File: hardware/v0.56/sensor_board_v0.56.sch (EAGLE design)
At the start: 67 parts, among them J3 USB-MICROB, U1 NEOPIXEL_NANO_2427, U10 TSL2591, U11 915MHz, U12 MH-Z19, U13 CCS811-I2C, U14 IAQ-CORE-C, U15 VLP-450-F, U16 VLP-450-F, U2 FT231XQ-R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

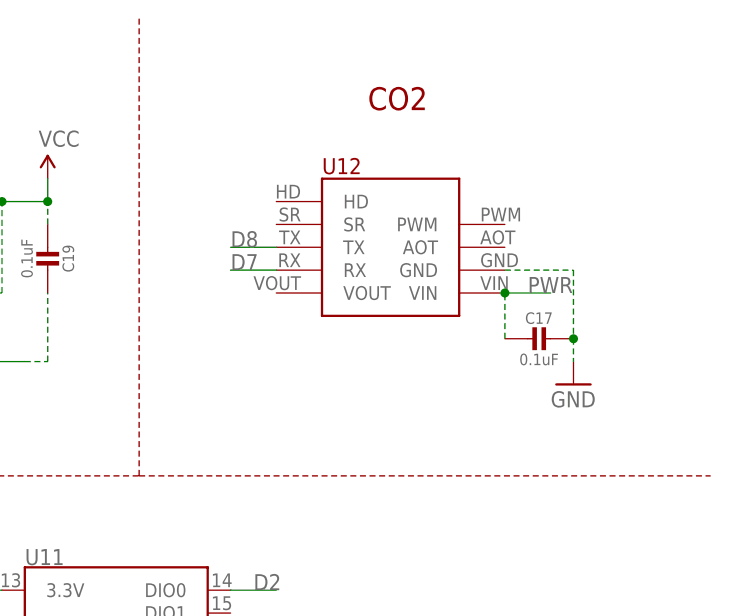
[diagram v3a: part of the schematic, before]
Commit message: Updated v0.56b with SMD pads for MH-z19 sensor
- other minor trace, parts and silkscreen adjustments
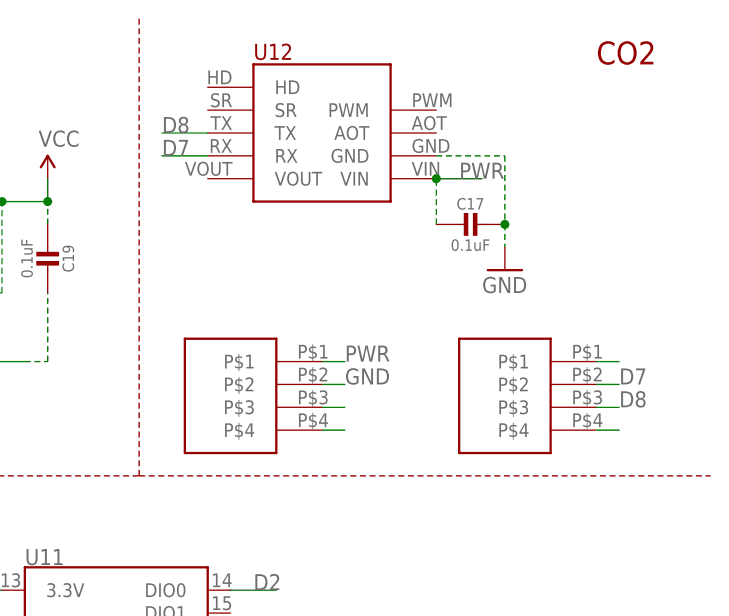
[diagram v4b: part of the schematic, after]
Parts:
- added U$4, U$5: 0878980426, 0878980426:0878980426
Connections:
- new net N$12: U$4.P$4
- new net N$14: U$5.P$1
- new net N$19: U$5.P$4
- new net N$8: U$4.P$3
- net D7: now also U$5.P$2
- net D8: now also U$5.P$3
- net GND: now also U$4.P$2
- net PWR: now also U$4.P$1
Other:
- moved on the sheet: C17, U12
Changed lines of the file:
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@@
 <part name="R10" library="Adafruit Feather 32u4 Bluefruit LE" deviceset="MICROBUILDER_RESISTOR" device="_0402MP" value="10K"/>
 <part name="SUPPLY18" library="SparkFun-Aesthetics" deviceset="VCC" device=""/>
+<part name="U$4" library="0878980426" deviceset="0878980426" device=""/>
+<part name="U$5" library="0878980426" deviceset="0878980426" device=""/>
 </parts>
 <sheets>
@@
 <wire x1="218.44" y1="-66.04" x2="218.44" y2="-12.7" width="0.1524" layer="94" style="longdash"/>
 <wire x1="251.46" y1="88.9" x2="251.46" y2="139.7" width="0.1524" layer="94" style="longdash"/>
-<text x="276.86" y="129.54" size="2.54" layer="94" font="vector">CO2</text>
+<text x="302.26" y="134.62" size="2.54" layer="94" font="vector">CO2</text>
 <wire x1="218.44" y1="-66.04" x2="312.42" y2="-66.04" width="0.1524" layer="94" style="longdash"/>
 <wire x1="53.34" y1="-12.7" x2="53.34" y2="43.18" width="0.1524" layer="94" style="longdash"/>
@@
 <instance part="R20" gate="G$1" x="172.72" y="-55.88" rot="R180"/>
 <instance part="J2" gate="G$1" x="157.48" y="-5.08"/>
-<instance part="U12" gate="G$1" x="279.4" y="114.3">
-<attribute name="MPN" x="279.4" y="114.3" size="1.778" layer="96" display="off"/>
+<instance part="U12" gate="G$1" x="271.78" y="127">
+<attribute name="MPN" x="271.78" y="127" size="1.778" layer="96" display="off"/>
 </instance>
 <instance part="U5" gate="G$1" x="-7.62" y="-71.12"/>
@@
 <instance part="C16" gate="G$1" x="10.16" y="111.76" rot="R180"/>
 <instance part="U13" gate="G$1" x="71.12" y="0"/>
-<instance part="GND14" gate="1" x="299.72" y="99.06"/>
-<instance part="C17" gate="G$1" x="294.64" y="104.14" rot="R270"/>
+<instance part="GND14" gate="1" x="292.1" y="111.76"/>
+<instance part="C17" gate="G$1" x="287.02" y="116.84" rot="R270"/>
 <instance part="JP1" gate="G$1" x="269.24" y="66.04" rot="R90"/>
 <instance part="U1" gate="G$1" x="147.32" y="63.5"/>
@@
 <instance part="R10" gate="G$1" x="101.6" y="99.06" rot="R90"/>
 <instance part="SUPPLY18" gate="G$1" x="111.76" y="96.52"/>
+<instance part="U$4" gate="G$1" x="259.08" y="101.6"/>
+<instance part="U$5" gate="G$1" x="289.56" y="101.6"/>
 </instances>
 <busses>
@@
 <pinref part="U12" gate="G$1" pin="GND"/>
 <pinref part="GND14" gate="1" pin="GND"/>
-<wire x1="292.1" y1="111.76" x2="299.72" y2="111.76" width="0.1524" layer="91" style="longdash"/>
-<wire x1="299.72" y1="111.76" x2="299.72" y2="104.14" width="0.1524" layer="91" style="longdash"/>
+<wire x1="284.48" y1="124.46" x2="292.1" y2="124.46" width="0.1524" layer="91" style="longdash"/>
+<wire x1="292.1" y1="124.46" x2="292.1" y2="116.84" width="0.1524" layer="91" style="longdash"/>
 <pinref part="C17" gate="G$1" pin="1"/>
-<wire x1="299.72" y1="104.14" x2="299.72" y2="101.6" width="0.1524" layer="91" style="longdash"/>
-<junction x="299.72" y="104.14"/>
+<wire x1="292.1" y1="116.84" x2="292.1" y2="114.3" width="0.1524" layer="91" style="longdash"/>
+<junction x="292.1" y="116.84"/>
 </segment>
 <segment>
@@
 <pinref part="C5" gate="G$1" pin="1"/>
 <wire x1="38.1" y1="-78.74" x2="38.1" y2="-76.2" width="0.1524" layer="91"/>
+</segment>
+<segment>
+<pinref part="U$4" gate="G$1" pin="P$2"/>
+<wire x1="271.78" y1="99.06" x2="274.32" y2="99.06" width="0.1524" layer="91"/>
+<label x="274.32" y="99.06" size="1.778" layer="95"/>
 </segment>
 </net>
@@
 <segment>
 <pinref part="U12" gate="G$1" pin="VIN"/>
-<label x="294.64" y="109.22" size="1.778" layer="95"/>
-<wire x1="292.1" y1="109.22" x2="297.18" y2="109.22" width="0.1524" layer="91"/>
+<label x="287.02" y="121.92" size="1.778" layer="95"/>
+<wire x1="284.48" y1="121.92" x2="289.56" y2="121.92" width="0.1524" layer="91"/>
 <pinref part="C17" gate="G$1" pin="2"/>
-<wire x1="292.1" y1="104.14" x2="292.1" y2="109.22" width="0.1524" layer="91" style="longdash"/>
-<junction x="292.1" y="109.22"/>
+<wire x1="284.48" y1="116.84" x2="284.48" y2="121.92" width="0.1524" layer="91" style="longdash"/>
+<junction x="284.48" y="121.92"/>
+</segment>
+<segment>
+<pinref part="U$4" gate="G$1" pin="P$1"/>
+<wire x1="271.78" y1="101.6" x2="274.32" y2="101.6" width="0.1524" layer="91"/>
+<label x="274.32" y="101.6" size="1.778" layer="95"/>
 </segment>
 </net>
@@
 <segment>
 <pinref part="U12" gate="G$1" pin="RX"/>
-<wire x1="266.7" y1="111.76" x2="261.62" y2="111.76" width="0.1524" layer="91"/>
-<label x="261.62" y="111.76" size="1.778" layer="95"/>
+<wire x1="259.08" y1="124.46" x2="254" y2="124.46" width="0.1524" layer="91"/>
+<label x="254" y="124.46" size="1.778" layer="95"/>
+</segment>
+<segment>
+<pinref part="U$5" gate="G$1" pin="P$2"/>
+<wire x1="302.26" y1="99.06" x2="304.8" y2="99.06" width="0.1524" layer="91"/>
+<label x="304.8" y="99.06" size="1.778" layer="95"/>
 </segment>
 </net>
@@
 <segment>
 <pinref part="U12" gate="G$1" pin="TX"/>
-<wire x1="266.7" y1="114.3" x2="261.62" y2="114.3" width="0.1524" layer="91"/>
-<label x="261.62" y="114.3" size="1.778" layer="95"/>
+<wire x1="259.08" y1="127" x2="254" y2="127" width="0.1524" layer="91"/>
+<label x="254" y="127" size="1.778" layer="95"/>
+</segment>
+<segment>
+<pinref part="U$5" gate="G$1" pin="P$3"/>
+<wire x1="302.26" y1="96.52" x2="304.8" y2="96.52" width="0.1524" layer="91"/>
+<label x="304.8" y="96.52" size="1.778" layer="95"/>
 </segment>
 </net>
@@
 </segment>
 </net>
+<net name="N$8" class="0">
+<segment>
+<pinref part="U$4" gate="G$1" pin="P$3"/>
+<wire x1="271.78" y1="96.52" x2="274.32" y2="96.52" width="0.1524" layer="91"/>
+</segment>
+</net>
+<net name="N$12" class="0">
+<segment>
+<pinref part="U$4" gate="G$1" pin="P$4"/>
+<wire x1="271.78" y1="93.98" x2="274.32" y2="93.98" width="0.1524" layer="91"/>
+</segment>
+</net>
+<net name="N$14" class="0">
+<segment>
+<pinref part="U$5" gate="G$1" pin="P$1"/>
+<wire x1="302.26" y1="101.6" x2="304.8" y2="101.6" width="0.1524" layer="91"/>
+</segment>
+</net>
+<net name="N$19" class="0">
+<segment>
+<pinref part="U$5" gate="G$1" pin="P$4"/>
+<wire x1="302.26" y1="93.98" x2="304.8" y2="93.98" width="0.1524" layer="91"/>
+</segment>
+</net>

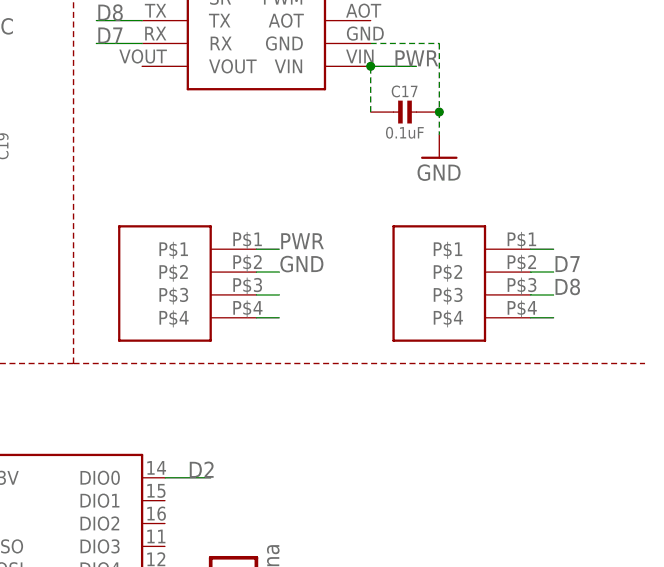
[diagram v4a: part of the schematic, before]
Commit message: v0.56b - minor update
silkscreen update and a couple of traces
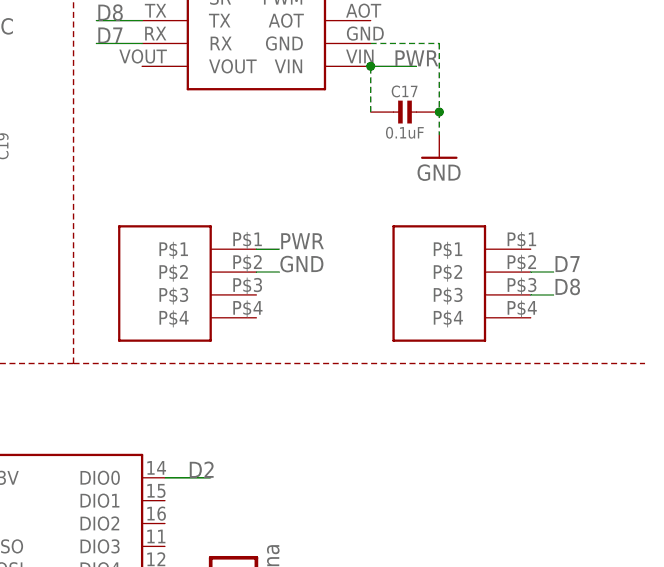
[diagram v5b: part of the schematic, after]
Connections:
- removed net N$12: U$4.P$4
- removed net N$14: U$5.P$1
- removed net N$19: U$5.P$4
- removed net N$8: U$4.P$3
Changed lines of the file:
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@@
-</segment>
-</net>
-<net name="N$8" class="0">
-<segment>
-<pinref part="U$4" gate="G$1" pin="P$3"/>
-<wire x1="271.78" y1="96.52" x2="274.32" y2="96.52" width="0.1524" layer="91"/>
-</segment>
-</net>
-<net name="N$12" class="0">
-<segment>
-<pinref part="U$4" gate="G$1" pin="P$4"/>
-<wire x1="271.78" y1="93.98" x2="274.32" y2="93.98" width="0.1524" layer="91"/>
-</segment>
-</net>
-<net name="N$14" class="0">
-<segment>
-<pinref part="U$5" gate="G$1" pin="P$1"/>
-<wire x1="302.26" y1="101.6" x2="304.8" y2="101.6" width="0.1524" layer="91"/>
-</segment>
-</net>
-<net name="N$19" class="0">
-<segment>
-<pinref part="U$5" gate="G$1" pin="P$4"/>
-<wire x1="302.26" y1="93.98" x2="304.8" y2="93.98" width="0.1524" layer="91"/>
 </segment>
 </net>
